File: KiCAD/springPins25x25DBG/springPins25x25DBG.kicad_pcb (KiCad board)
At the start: 2 copper layers, 30 x 30 mm, 22 parts, among them J1 CONN_02X06, J2 CONN_02X06

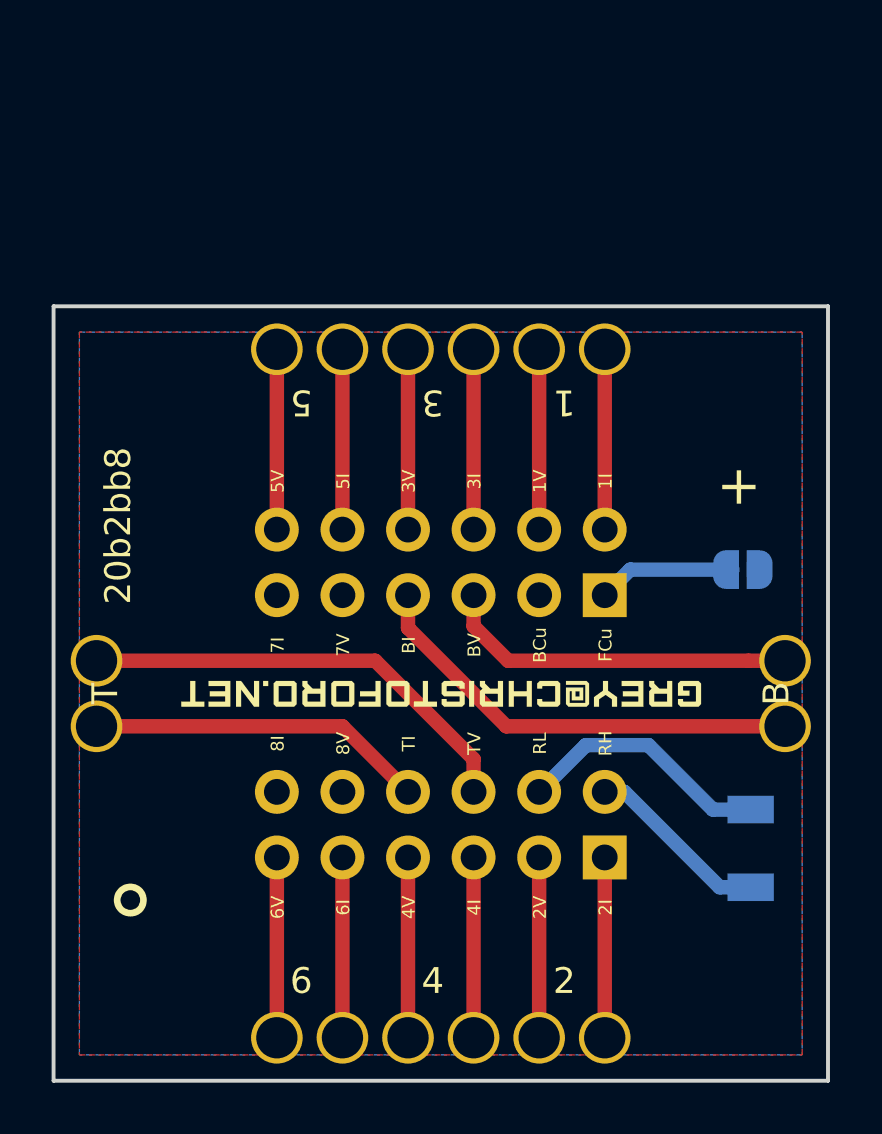
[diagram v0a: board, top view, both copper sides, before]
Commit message: add dbg adapter
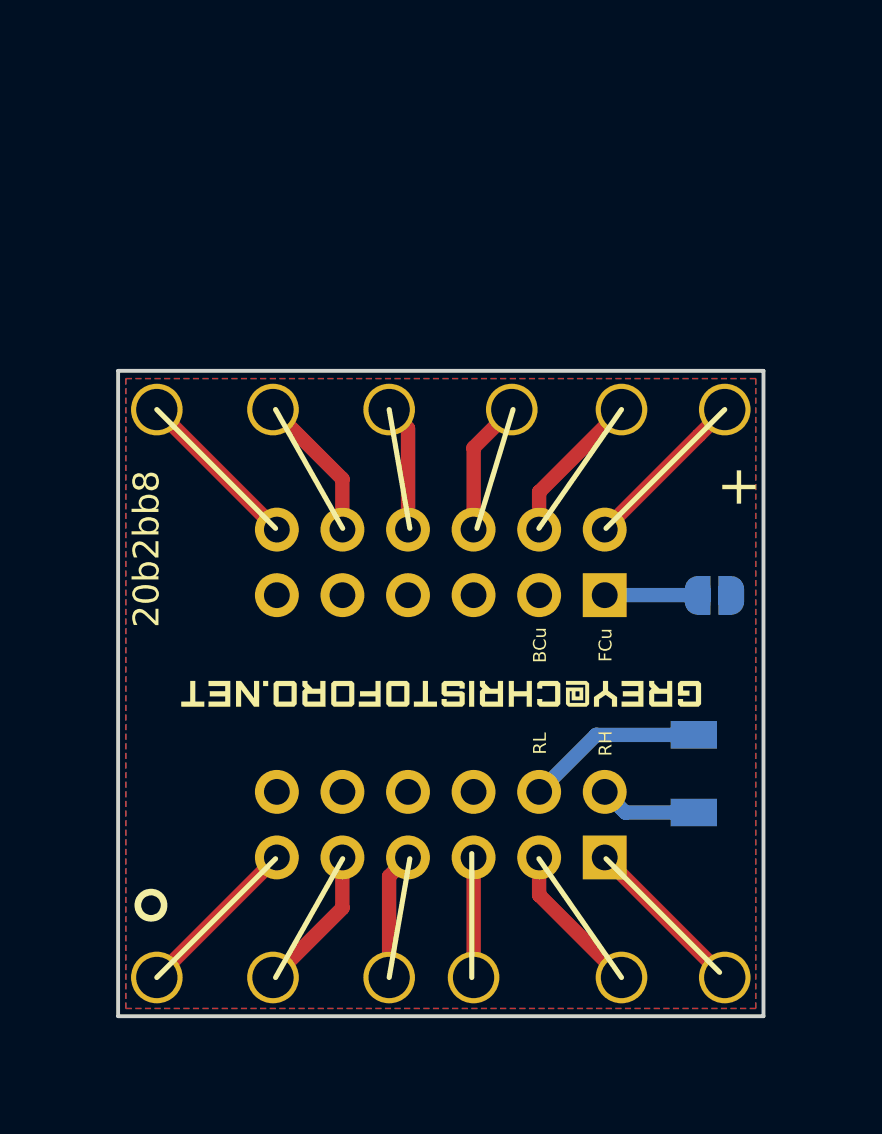
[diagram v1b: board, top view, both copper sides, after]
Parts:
- removed TP10, TP11, TP12, TP9: TEST, myParts:S25-022+P25-4023
- moved TP15 5.20 mm to (-11.0, -11.0)
- moved TP20 5.20 mm to (11.0, -11.0)
- moved TP3 5.20 mm to (-11.0, 11.0)
- moved TP8 5.20 mm to (11.0, 11.0)
- moved TP19 3.95 mm to (7.00, -11.0)
- moved TP7 3.95 mm to (7.00, 11.0)
- moved R1 3.64 mm to (9.80, 3.10)
- moved TP16 3.56 mm to (-6.50, -11.0)
- moved TP4 3.56 mm to (-6.50, 11.0)
- moved TP18 2.76 mm to (2.75, -11.0), turned to 0 degrees
- moved TP17 2.45 mm to (-2.00, -11.0)
- moved TP5 2.45 mm to (-2.00, 11.0)
- moved TP6 2.34 mm to (1.27, 11.0)
- moved JP1 1.49 mm to (10.6, -3.80)
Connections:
- net /I1 renamed /R6
- net /I2 renamed /L6
- net /I3 renamed /R4
- net /I4 renamed /L4
- net /I5 renamed /R2
- net /I6 renamed /L2
- net /V1 renamed /R5
- net /V2 renamed /L5
- net /V3 renamed /R3
- net /V4 renamed /L3
- net /V5 renamed /R1
- net /V6 renamed /L1
- J1 pad 6: /VT -> Net-(J1-Pad6)
- J1 pad 8: /IT -> Net-(J1-Pad8)
- J2 pad 5: /VB -> Net-(J2-Pad5)
- J2 pad 7: /IB -> Net-(J2-Pad7)
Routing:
- net /VT: track 17.5 -> 0.00 mm
- net /IB: track 17.5 -> 0.00 mm
- net /VB: track 13.8 -> 0.00 mm
- net /IT: track 13.1 -> 0.00 mm
- net /RH: track 7.18 -> 3.78 mm
- net /RL: track 9.97 -> 6.91 mm
- net /L4: track 6.99 -> 4.65 mm
- net /R3: track 6.99 -> 4.95 mm
- net /L3: track 6.99 -> 4.95 mm
- net /FCu: track 5.36 -> 3.60 mm
- net /R4: track 6.99 -> 5.26 mm
- net /R2: track 6.99 -> 5.76 mm
- net /L2: track 6.99 -> 5.76 mm
- net /R5: track 6.99 -> 5.97 mm
- net /L5: track 6.99 -> 5.97 mm
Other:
- board size 30 x 30 mm -> 25 x 25 mm
- board text removed: "1"
- board text removed: "1I"
- board text removed: "1V"
- board text removed: "2"
- board text removed: "2I"
- board text removed: "2V"
- board text removed: "3"
- board text removed: "3I"
- board text removed: "3V"
- board text removed: "4"
- board text removed: "4I"
- board text removed: "4V"
- board text removed: "5"
- board text removed: "5I"
- board text removed: "5V"
- board text removed: "6"
- board text removed: "6I"
- board text removed: "6V"
- board text removed: "7I"
- board text removed: "7V"
- board text removed: "8I"
- board text removed: "8V"
- board text removed: "B"
- board text removed: "BI"
- board text removed: "BV"
- board text removed: "T"
- board text removed: "TI"
- board text removed: "TV"

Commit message: update silk before order 629bf0f
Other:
- board text added: "629bf0f"
- board text removed: "20b2bb8"
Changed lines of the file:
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@@
   )
   (setup
-    (last_trace_width 0.56)
+    (last_trace_width 0.25)
     (user_trace_width 0.2)
     (user_trace_width 0.56)
@@
     (effects (font (size 1.5 1.5) (thickness 0.3)))
   )
-  (gr_text 20b2bb8 (at -11.4 -5.6 90) (layer F.SilkS)
+  (gr_text 629bf0f (at -11.4 -5.6 90) (layer F.SilkS)
     (effects (font (size 1 1) (thickness 0.175)))
   )

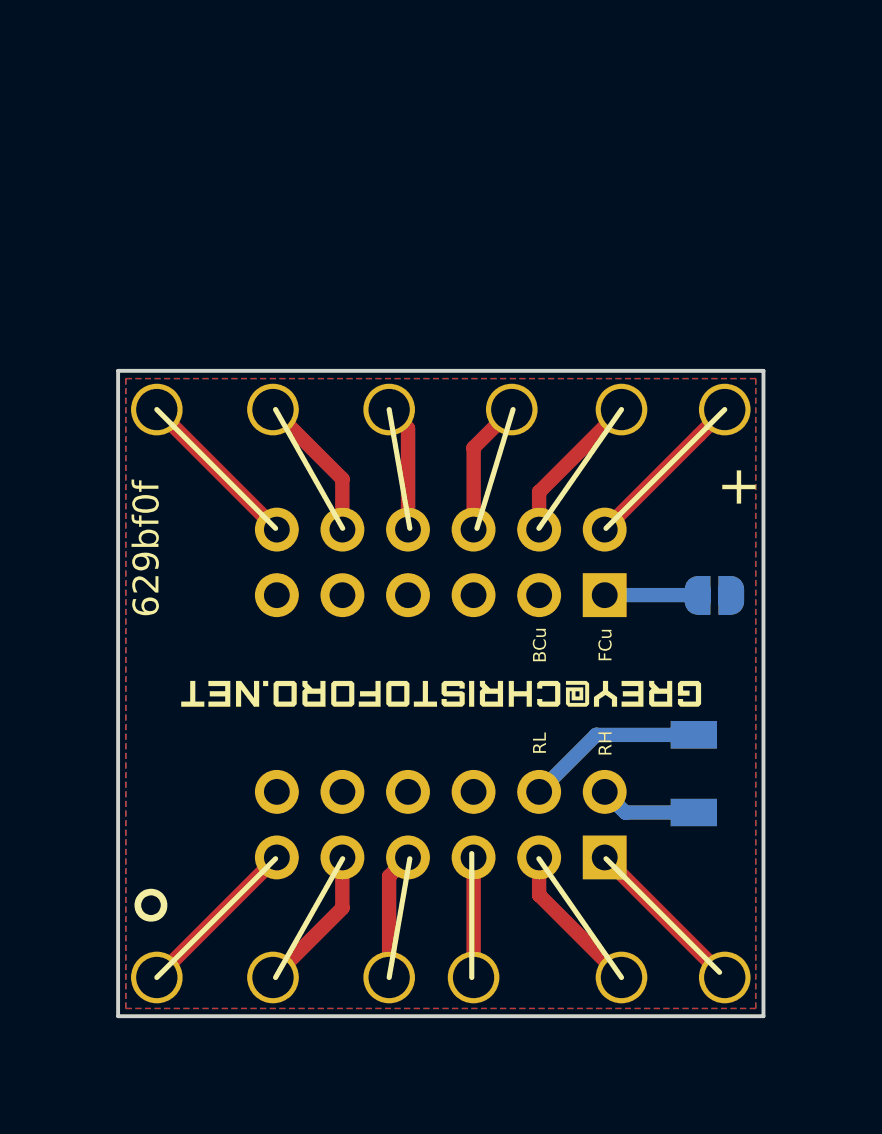
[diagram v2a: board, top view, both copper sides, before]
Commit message: fix dbg board adapter
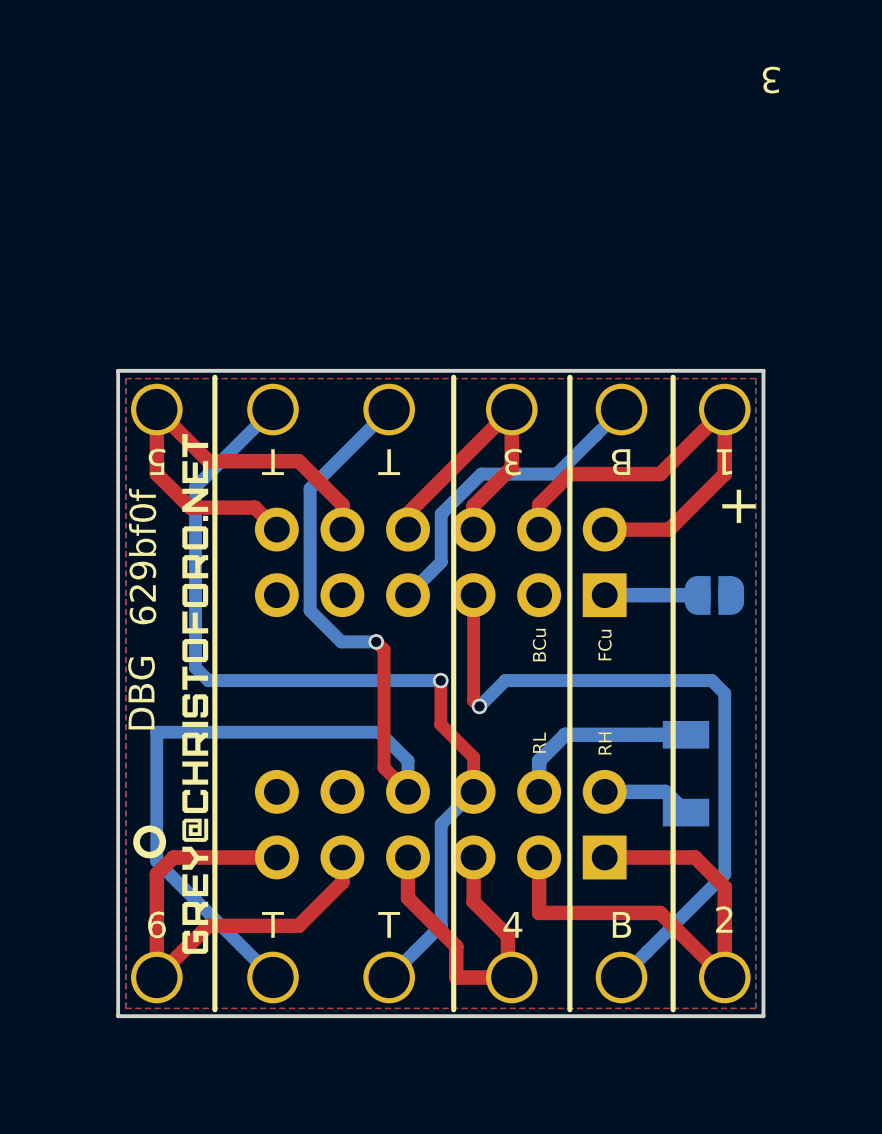
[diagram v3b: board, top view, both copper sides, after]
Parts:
- moved L1 9.50 mm to (-9.50, 0.00), turned to 270 degrees
- moved L1 9.50 mm to (-9.50, 0.00), turned to 90 degrees
- moved TP6 1.48 mm to (2.75, 11.0)
- moved R1 0.30 mm to (9.50, 3.10)
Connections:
- net Net-(J1-Pad10) renamed /V8
- net Net-(J1-Pad12) renamed /I8
- net Net-(J2-Pad11) renamed /I7
- net Net-(J2-Pad9) renamed /V7
- J1 pad 1: /L6 -> /I2
- J1 pad 11: /L1 -> /I6
- J1 pad 3: /L5 -> /I2
- J1 pad 5: /L4 -> /I4
- J1 pad 6: Net-(J1-Pad6) -> /VT
- J1 pad 7: /L3 -> /I4
- J1 pad 8: Net-(J1-Pad8) -> /IT
- J1 pad 9: /L2 -> /I6
- J2 pad 10: /R2 -> /I5
- J2 pad 12: /R1 -> /I5
- J2 pad 2: /R6 -> /I1
- J2 pad 4: /R5 -> /I1
- J2 pad 5: Net-(J2-Pad5) -> /VB
- J2 pad 6: /R4 -> /I3
- J2 pad 7: Net-(J2-Pad7) -> /IB
- J2 pad 8: /R3 -> /I3
- TP15 pad 1: /R1 -> /I5
- TP16 pad 1: /R2 -> /VT
- TP17 pad 1: /R3 -> /IT
- TP18 pad 1: /R4 -> /I3
- TP19 pad 1: /R5 -> /IB
- TP20 pad 1: /R6 -> /I1
- TP3 pad 1: /L1 -> /I6
- TP4 pad 1: /L2 -> /IT
- TP5 pad 1: /L3 -> /VT
- TP6 pad 1: /L4 -> /I4
- TP7 pad 1: /L5 -> /VB
- TP8 pad 1: /L6 -> /I2
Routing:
- net /IT: track 0.00 -> 41.2 mm, vias 0 -> 1
- net /VT: track 0.00 -> 34.3 mm, vias 0 -> 1
- net /VB: track 0.00 -> 27.2 mm, vias 0 -> 1
- net /I2: track 0.00 -> 19.0 mm
- net /I6: track 0.00 -> 18.6 mm
- net /I5: track 0.00 -> 17.7 mm
- net /I1: track 0.00 -> 17.7 mm
- net /I4: track 0.00 -> 12.8 mm
- net /IB: track 0.00 -> 12.3 mm
- net /I3: track 0.00 -> 11.6 mm
- net /R1: track 6.58 -> 0.00 mm
- net /L6: track 6.58 -> 0.00 mm
- net /L1: track 6.58 -> 0.00 mm
- net /R6: track 6.58 -> 0.00 mm
- net /R5: track 5.97 -> 0.00 mm
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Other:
- board text added: "1"
- board text added: "2"
- board text added: "3"
- board text added: "4"
- board text added: "5"
- board text added: "6"
- board text added: "B"
- board text added: "DBG ~"
- board text added: "T"

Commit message: add substrate markers
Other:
- board text added: "b2b8b2c"
- board text removed: "629bf0f"
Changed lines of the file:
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@@
   )
   (setup
-    (last_trace_width 0.56)
+    (last_trace_width 0.25)
     (user_trace_width 0.2)
     (user_trace_width 0.5)
@@
     (effects (font (size 1.5 1.5) (thickness 0.3)))
   )
-  (gr_text 629bf0f (at -11.5 -5.25 90) (layer F.SilkS)
-    (effects (font (size 1 1) (thickness 0.175)))
-  )
+  (gr_text b2b8b2c (at -11.5 -5.25 90) (layer F.SilkS)
+    (effects (font (size 1 1) (thickness 0.175)))
+  )

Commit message: update silk
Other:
- board text added: "779dfac"
- board text removed: "b2b8b2c"
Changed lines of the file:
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@@
     (effects (font (size 1.5 1.5) (thickness 0.3)))
   )
-  (gr_text b2b8b2c (at -11.5 -5.25 90) (layer F.SilkS)
+  (gr_text 779dfac (at -11.5 -5.25 90) (layer F.SilkS)
     (effects (font (size 1 1) (thickness 0.175)))
   )
